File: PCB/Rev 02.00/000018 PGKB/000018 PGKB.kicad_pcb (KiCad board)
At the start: 2 copper layers, 93.5 x 72.5 mm, 140 parts, among them J1 USB Mini B, J2 BM04B-SRSS-TB, U1 SN74HCS365PWR, U2 SN74HCS365PWR, U3 SN74HCS365PWR, U4 W25Q80DVSSIG, U5 RP2040, U6 MCP1825T-3302E/DC, U7 CAT811TTBI-GT3, Y1 12 MHz

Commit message: 4L board
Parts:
- moved C27 8.23 mm to (70.3, 145.7), turned to 180 degrees
- moved C30 5.70 mm to (68.7, 137.6), turned to 0 degrees
- moved C2 0.67 mm to (89.9, 113.8)
- moved FB1 0.67 mm to (91.7, 114.0)
- moved D12 0.52 mm to (94.0, 114.0)
- moved R25 0.44 mm to (68.7, 136.1), turned to 0 degrees
- turned Y1 to 180 degrees
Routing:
- net /Main/Memory/CLK: track 0.00 -> 46.8 mm, vias 0 -> 2
- net /Main/Memory/DATA3: track 0.00 -> 46.1 mm, vias 0 -> 2
- net /Main/Memory/DATA0: track 0.00 -> 45.2 mm, vias 0 -> 2
- net /Main/Memory/DATA1: track 0.00 -> 40.9 mm, vias 0 -> 2
- net /Main/Memory/DATA2: track 0.00 -> 39.3 mm, vias 0 -> 2
- net /Main/Microcontroller/USB_MCU_D_P: track 0.00 -> 32.8 mm, vias 0 -> 2
- net /Main/Microcontroller/USB_MCU_D_N: track 0.00 -> 32.3 mm, vias 0 -> 2
- net Net-(U5-ADC_AVDD): track 4.73 -> 26.5 mm
- net /Main/USB Connector/USB_D_N: track 0.00 -> 15.4 mm
- net /Main/USB Connector/USB_D_P: track 0.00 -> 15.3 mm
- net Net-(U5-XIN): track 0.00 -> 11.5 mm
- net Net-(D10-DIN): track 0.00 -> 7.93 mm
- net GND: track 0.00 -> 7.20 mm, vias 0 -> 6
- net Net-(U5-XOUT): track 0.00 -> 3.47 mm
- added copper zone on In1.Cu, net GND
- added copper zone on In2.Cu, net GND
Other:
- copper layers 2 -> 4

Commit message: Leiskaa
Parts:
- removed FB3: Ferrite_500mA_TDK_MMZ2012Y152BT000, KD_Inductor:INDC2016X100N
- added ART1: 4-Layer Marking, KD_Mechanical:ART_4-LAYER, F.Cu at (53.4, 172.0)
- added ART2: Logo 2.5 mm Silk, KD_Mechanical:ART_LOGO_TEXT_2.5MM_SILK, F.Cu at (78.9, 172.5)
- added C3: 10n, KD_Capacitor:CAPC1608X90N, B.Cu at (81.6, 150.7)
- added R29: 10k, KD_Resistor:RESC1608X55N, B.Cu at (117.0, 115.5)
- FB2: value Ferrite_300mA_Abracon_ACML-0805-102-T -> Ferrite_500mA_TDK_MMZ2012Y152BT000
- H3: value NPTH 3.2 M3 Clearance -> NPTH_3.2; footprint KD_Mechanical_Mounting_Hole:NPTH_3.2mm_M3_clearance -> KD_Mechanical_Mounting_Hole:NPTH_3.2mm
- R15, R16, R17: value R_0603_1k_1% -> 1k
- R24: value R_0603_22k_1% -> R_0603_DNP
- R26, R27: value 4k7 -> R_0603_5100_1%; footprint KD_Resistor:RESC1005X40N -> KD_Resistor:RESC1608X55N
- TP9: moved to B.Cu
- moved C14 33.0 mm to (91.8, 142.1), turned to -90 degrees
- moved FB2 21.9 mm to (77.1, 127.0), turned to 180 degrees
- moved C41 21.7 mm to (113.3, 130.2), turned to 180 degrees
- moved R28 21.3 mm to (113.3, 128.7), turned to 0 degrees
- moved R22 20.6 mm to (53.3, 107.6), turned to 90 degrees
- moved TP2 19.4 mm to (95.8, 151.2)
- moved TP6 15.6 mm to (49.9, 126.7)
- moved R24 12.0 mm to (83.1, 150.7), turned to -90 degrees
- moved TP8 10.3 mm to (66.8, 145.2)
- moved TP14 7.02 mm to (126.4, 127.2)
- moved C32 6.70 mm to (57.7, 129.9), turned to 90 degrees
- moved TP11 4.46 mm to (66.3, 106.6)
- moved TP12 4.17 mm to (70.6, 106.6)
- moved R27 3.32 mm to (71.7, 115.8)
- moved C39 3.20 mm to (100.1, 109.1)
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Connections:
- net Net-(U5-ADC_AVDD) renamed /Main/Microcontroller/3V3_MCU
- C14 pad 1: +3.3V -> +3V3
- C15 pad 1: +3.3V -> +3V3
- J2 pad 3: /Main/Connectors/SDA -> /Main/Connectors/I2C1_SDA
- J2 pad 4: /Main/Connectors/SCL -> /Main/Connectors/I2C1_SCL
- R15 pad 1: +3.3V -> +3V3
- R16 pad 1: +3.3V -> +3V3
- R17 pad 1: +3.3V -> +3V3
- R26 pad 2: /Main/Microcontroller/SDA -> /Main/Connectors/I2C1_SDA
- R27 pad 2: /Main/Microcontroller/SCL -> /Main/Connectors/I2C1_SCL
- S1 pad 1: +3.3V -> +3V3
- S10 pad 1: +3.3V -> +3V3
- S11 pad 1: +3.3V -> +3V3
- S2 pad 1: +3.3V -> +3V3
- S3 pad 1: +3.3V -> +3V3
- S4 pad 1: +3.3V -> +3V3
- S5 pad 1: +3.3V -> +3V3
- S6 pad 1: +3.3V -> +3V3
- S7 pad 1: +3.3V -> +3V3
- S8 pad 1: +3.3V -> +3V3
- S9 pad 1: +3.3V -> +3V3
- TP11 pad 1: /Main/Microcontroller/SCL -> /Main/Connectors/I2C1_SDA
- TP12 pad 1: /Main/Microcontroller/SDA -> /Main/Connectors/I2C1_SCL
- U1 pad 16: +3.3V -> +3V3
- U2 pad 16: +3.3V -> +3V3
- U3 pad 16: +3.3V -> +3V3
- U5 pad 34: /Main/Microcontroller/I2C1_SDA -> /Main/Connectors/I2C1_SDA
- U5 pad 35: /Main/Microcontroller/I2C1_SCL -> /Main/Connectors/I2C1_SCL
- U5 pad 39: /Main/Microcontroller/GPIO10 -> /Main/Buttons/Button10
- U5 pad 40: /Main/Microcontroller/GPIO11 -> /Main/Buttons/Button11
- U6 pad 1: PERIP_~{RESET} -> /Main/Neopixel LEDs/NEOPIXEL_VDD
- U6 pad 4: Net-(U6-VO) -> +3V3
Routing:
- net +3V3: track 0.00 -> 438.0 mm, vias 0 -> 16
- net /Main/Neopixel LEDs/NEOPIXEL_VDD: track 0.00 -> 287.4 mm, vias 0 -> 12
- net GND: track 7.20 -> 138.1 mm, vias 6 -> 56
- net /Main/Memory/~{CS}_MEMORY: track 0.00 -> 112.4 mm, vias 0 -> 5
- net /Main/Microcontroller/~{RESET}: track 0.00 -> 110.2 mm, vias 0 -> 5
- net Net-(D4-DOUT): track 0.00 -> 104.3 mm, vias 0 -> 2
- net Net-(D8-DOUT): track 0.00 -> 97.6 mm, vias 0 -> 2
- net /Main/Connectors/I2C1_SDA: track 0.00 -> 63.5 mm, vias 0 -> 2
- net Net-(U1-I1): track 0.00 -> 63.3 mm, vias 0 -> 4
- net /Main/Buttons/Button8: track 0.00 -> 61.0 mm, vias 0 -> 3
- net /Main/Buttons/Button7: track 0.00 -> 59.1 mm, vias 0 -> 3
- net /Main/Connectors/I2C1_SCL: track 0.00 -> 58.7 mm, vias 0 -> 2
- net /Main/Buttons/Button4: track 0.00 -> 55.2 mm, vias 0 -> 3
- net /Main/Microcontroller/ENC_B: track 0.00 -> 54.9 mm, vias 0 -> 2
- net Net-(U3-I3): track 0.00 -> 54.4 mm, vias 0 -> 2
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- added copper zone on B.Cu, net GND
- added copper zone on F.Cu, net GND

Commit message: error fixing
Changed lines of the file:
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@@
     (property "ki_keywords" "test point testpoint")
     (attr exclude_from_pos_files exclude_from_bom)
-    (fp_text reference "TP11" (at 0 2.148) (layer "B.SilkS")
-        (effects (font (size 0.8 0.8) (thickness 0.15)) (justify mirror))
+    (fp_text reference "TP11" (at 0 -2.2) (layer "F.SilkS")
+        (effects (font (size 0.8 0.8) (thickness 0.15)))
     )
     (fp_text value "TP D2.5 mm H0.9mm" (at 0 -2.25) (layer "B.Fab") hide
@@
     (property "ki_keywords" "test point testpoint")
     (attr exclude_from_pos_files exclude_from_bom)
-    (fp_text reference "TP12" (at 0 2.148 90) (layer "B.SilkS")
-        (effects (font (size 0.8 0.8) (thickness 0.15)) (justify mirror))
+    (fp_text reference "TP12" (at 2.2 0) (layer "F.SilkS")
+        (effects (font (size 0.8 0.8) (thickness 0.15)))
     )
     (fp_text value "TP D2.5 mm H0.9mm" (at 0 -2.25 90) (layer "B.Fab") hide
@@
     (property "ki_keywords" "test point testpoint")
     (attr exclude_from_pos_files exclude_from_bom)
-    (fp_text reference "TP7" (at 0 2.148 90) (layer "B.SilkS")
+    (fp_text reference "TP7" (at 2.300674 -0.950211 -180) (layer "B.SilkS")
         (effects (font (size 0.8 0.8) (thickness 0.15)) (justify mirror))
     )
@@
         (effects (font (size 0.5 0.5) (thickness 0.1)) (justify mirror))
     )
-    (fp_line (start -1.62 -8.73) (end 7.57 -8.73)
-      (stroke (width 0.12) (type solid)) (layer "B.SilkS"))
-    (fp_line (start -1.62 -6) (end -1.62 -8.73)
-      (stroke (width 0.12) (type solid)) (layer "B.SilkS"))
     (fp_line (start -1.62 -2.4) (end -1.62 -3.3)
       (stroke (width 0.12) (type solid)) (layer "B.SilkS"))
     (fp_line (start -1.5 0.68) (end 7.45 0.68)
       (stroke (width 0.12) (type solid)) (layer "B.SilkS"))
-    (fp_line (start 7.57 -6) (end 7.57 -8.73)
-      (stroke (width 0.12) (type solid)) (layer "B.SilkS"))
     (fp_line (start 7.57 -2.4) (end 7.57 -3.3)
       (stroke (width 0.12) (type solid)) (layer "B.SilkS"))
@@
     (fp_line (start -1.5 -8.61) (end 7.45 -8.61)
       (stroke (width 0.1) (type solid)) (layer "B.Fab"))
+    (fp_line (start -1.5 -6.1) (end 1 -6.1)
+      (stroke (width 0.1) (type dot)) (layer "B.Fab"))
     (fp_line (start -1.5 0.56) (end -1.5 -8.61)
       (stroke (width 0.1) (type solid)) (layer "B.Fab"))
     (fp_line (start -1.5 0.56) (end 7.45 0.56)
       (stroke (width 0.1) (type solid)) (layer "B.Fab"))
-    (fp_line (start -0.025 -6.1) (end 5.975 -6.1)
-      (stroke (width 0.1) (type solid)) (layer "B.Fab"))
+    (fp_line (start 5 -6.1) (end 7.5 -6.1)
+      (stroke (width 0.1) (type dot)) (layer "B.Fab"))
     (fp_line (start 7.45 0.56) (end 7.45 -8.61)
       (stroke (width 0.1) (type solid)) (layer "B.Fab"))
@@
     (property "ki_keywords" "test point testpoint")
     (attr exclude_from_pos_files exclude_from_bom)
-    (fp_text reference "TP14" (at 0 2.148 270) (layer "B.SilkS")
+    (fp_text reference "TP14" (at -1 -3) (layer "B.SilkS")
         (effects (font (size 0.8 0.8) (thickness 0.15)) (justify mirror))
     )
@@
     (property "ki_keywords" "test point testpoint")
     (attr exclude_from_pos_files exclude_from_bom)
-    (fp_text reference "TP2" (at 0 2.148 90) (layer "B.SilkS")
+    (fp_text reference "TP2" (at -2.2 0.7 -180) (layer "B.SilkS")
         (effects (font (size 0.8 0.8) (thickness 0.15)) (justify mirror))
     )
@@
     (property "ki_keywords" "test point testpoint")
     (attr exclude_from_pos_files exclude_from_bom)
-    (fp_text reference "TP16" (at 0 2.148) (layer "B.SilkS")
+    (fp_text reference "TP16" (at -0.1 -2.3) (layer "B.SilkS")
         (effects (font (size 0.8 0.8) (thickness 0.15)) (justify mirror))
     )
@@
     (property "ki_keywords" "test point testpoint")
     (attr exclude_from_pos_files exclude_from_bom)
-    (fp_text reference "TP3" (at 0 2.148) (layer "B.SilkS")
+    (fp_text reference "TP3" (at 2.3 1.8) (layer "B.SilkS")
         (effects (font (size 0.8 0.8) (thickness 0.15)) (justify mirror))
     )
@@
         (xy 59.5 123)
         (xy 59.5 127)
-        (xy 59.5 127)
       )

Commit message: layout
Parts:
- C16, C17, C18: value C_0603_100n_X7R_50V -> 100n
- FD1, FD2, FD3, FD4, FD5, FD6: value Fiducial_0.5mm -> Fiducial 0.5 mm
- S12, S13: value Button_tactile_45x38_430181038816 -> 430181038816
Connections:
- U3 pad 10: unconnected-(U3-I4-Pad10) -> GND
- U3 pad 12: unconnected-(U3-I5-Pad12) -> GND
- U3 pad 14: unconnected-(U3-I6-Pad14) -> GND
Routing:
- net GND: track 138.1 -> 145.4 mm, vias 56 -> 57

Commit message: päivityksiä
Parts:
- added R30: 100k, KD_Resistor:RESC1608X55N, B.Cu at (161.6, 132.4)
- added R31: 100k, KD_Resistor:RESC1608X55N, B.Cu at (161.6, 134.9)
- added R34: 100k, KD_Resistor:RESC1608X55N, B.Cu at (161.6, 137.4)
- added R35: 100k, KD_Resistor:RESC1608X55N, B.Cu at (161.6, 139.9)
- added R36: 100k, KD_Resistor:RESC1608X55N, B.Cu at (161.6, 142.4)
- added R37: 100k, KD_Resistor:RESC1608X55N, B.Cu at (161.6, 144.9)
- added R38: 100k, KD_Resistor:RESC1608X55N, B.Cu at (157.6, 132.4)
- added R39: 100k, KD_Resistor:RESC1608X55N, B.Cu at (157.6, 134.9)
- added R40: 100k, KD_Resistor:RESC1608X55N, B.Cu at (157.6, 137.4)
- added R41: 100k, KD_Resistor:RESC1608X55N, B.Cu at (157.6, 139.9)
- added R42: 100k, KD_Resistor:RESC1608X55N, B.Cu at (157.6, 142.4)
- moved R2 3.11 mm to (80.8, 108.4)
- moved R1 3.11 mm to (82.4, 108.4)
- moved C21 0.90 mm to (76.6, 107.5)
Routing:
- net /Main/USB Connector/CC1: track 11.8 -> 8.97 mm
- net /Main/USB Connector/CC2: track 9.28 -> 11.0 mm
- net +3V3: track 438.0 -> 437.1 mm
- net GND: track 145.4 -> 145.3 mm, vias 57 -> 181

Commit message: Review checklists
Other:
- board text added: "000018 PGKB Rev 1.00"
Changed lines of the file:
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@@
     (fp_arc (start 0.833601 0.096099) (mid 0.973613 -0.257639) (end 1.31605 -0.423381)
       (stroke (width 0.2) (type solid)) (layer "F.SilkS"))
-    (fp_arc (start 1.31605 -0.683114) (mid 1.907699 -0.405492) (end 2.078018 0.225468)
+    (fp_arc (start 1.31605 -0.683114) (mid 1.907695 -0.405492) (end 2.078018 0.225468)
       (stroke (width 0.2) (type solid)) (layer "F.SilkS"))
     (fp_arc (start 1.31605 -0.423379) (mid 1.645394 -0.271037) (end 1.761468 0.072768)
@@
     (fp_arc (start 1.355618 1.232463) (mid 0.731987 0.965619) (end 0.50639 0.325909)
       (stroke (width 0.2) (type solid)) (layer "F.SilkS"))
-    (fp_arc (start 1.372869 0.972724) (mid 0.966364 0.781549) (end 0.82295 0.35584)
+    (fp_arc (start 1.372869 0.972724) (mid 0.966366 0.781547) (end 0.82295 0.35584)
       (stroke (width 0.2) (type solid)) (layer "F.SilkS"))
     (fp_arc (start 1.8609 0.725158) (mid 1.647116 0.90854) (end 1.372868 0.972731)
@@
     (fp_arc (start 3.12764 0.972723) (mid 2.834729 0.892832) (end 2.685781 0.628268)
       (stroke (width 0.2) (type solid)) (layer "F.SilkS"))
-    (fp_arc (start 3.12764 1.232463) (mid 2.619347 1.092399) (end 2.369218 0.628268)
+    (fp_arc (start 3.12764 1.232463) (mid 2.61934 1.092397) (end 2.369218 0.628268)
       (stroke (width 0.2) (type solid)) (layer "F.SilkS"))
-    (fp_arc (start 5.03409 0.259459) (mid 5.19195 -0.37288) (end 5.765118 -0.683118)
+    (fp_arc (start 5.03409 0.259459) (mid 5.191951 -0.372877) (end 5.765118 -0.683118)
       (stroke (width 0.2) (type solid)) (layer "F.SilkS"))
     (fp_arc (start 5.761569 1.232466) (mid 5.184943 0.905126) (end 5.03409 0.259459)
@@
     (fp_arc (start 5.844259 -0.423382) (mid 6.101988 -0.353589) (end 6.28105 -0.155518)
       (stroke (width 0.2) (type solid)) (layer "F.SilkS"))
-    (fp_arc (start 6.280538 1.013814) (mid 6.045436 1.181008) (end 5.761568 1.232468)
+    (fp_arc (start 6.280538 1.013814) (mid 6.045436 1.181019) (end 5.761568 1.232468)
       (stroke (width 0.2) (type solid)) (layer "F.SilkS"))
     (fp_arc (start 6.280541 1.169557) (mid 6.145913 1.523237) (end 5.79099 1.65455)
@@
     (fp_arc (start 7.400665 -0.416784) (mid 7.646446 -0.616044) (end 7.955659 -0.683118)
       (stroke (width 0.2) (type solid)) (layer "F.SilkS"))
-    (fp_arc (start 7.407765 -0.124568) (mid 7.589656 -0.340694) (end 7.859781 -0.423381)
+    (fp_arc (start 7.407765 -0.124568) (mid 7.589655 -0.340729) (end 7.859781 -0.423381)
       (stroke (width 0.2) (type solid)) (layer "F.SilkS"))
     (fp_arc (start 7.859779 -0.42338) (mid 8.138248 -0.314437) (end 8.231131 -0.030218)
       (stroke (width 0.2) (type solid)) (layer "F.SilkS"))
-    (fp_arc (start 7.955657 -0.683113) (mid 8.404847 -0.489303) (end 8.54819 -0.02159)
+    (fp_arc (start 7.955657 -0.683113) (mid 8.404805 -0.489301) (end 8.54819 -0.02159)
       (stroke (width 0.2) (type solid)) (layer "F.SilkS"))
     (fp_arc (start 9.023535 -0.141819) (mid 9.255576 -0.552139) (end 9.7084 -0.683118)
@@
     (fp_arc (start 9.708398 -0.683125) (mid 10.188203 -0.5481) (end 10.415081 -0.104281)
       (stroke (width 0.2) (type solid)) (layer "F.SilkS"))
-    (fp_arc (start 9.708398 -0.423378) (mid 9.96879 -0.344297) (end 10.097 -0.104281)
+    (fp_arc (start 9.708398 -0.423378) (mid 9.968762 -0.344292) (end 10.097 -0.104281)
       (stroke (width 0.2) (type solid)) (layer "F.SilkS"))
     (fp_arc (start 9.71855 0.972726) (mid 9.425639 0.892824) (end 9.276681 0.628268)
       (stroke (width 0.2) (type solid)) (layer "F.SilkS"))
-    (fp_arc (start 9.71855 1.232464) (mid 9.21027 1.092398) (end 8.960131 0.628268)
+    (fp_arc (start 9.71855 1.232464) (mid 9.210242 1.092402) (end 8.960131 0.628268)
       (stroke (width 0.2) (type solid)) (layer "F.SilkS"))
   )
@@
     (effects (font (size 1 1) (thickness 0.15)) (justify left bottom))
   )
+  (gr_text "000018 PGKB Rev 1.00" (at 98.5 172.2) (layer "F.SilkS")
+    (effects (font (size 1 1) (thickness 0.15)) (justify left bottom))
+  )

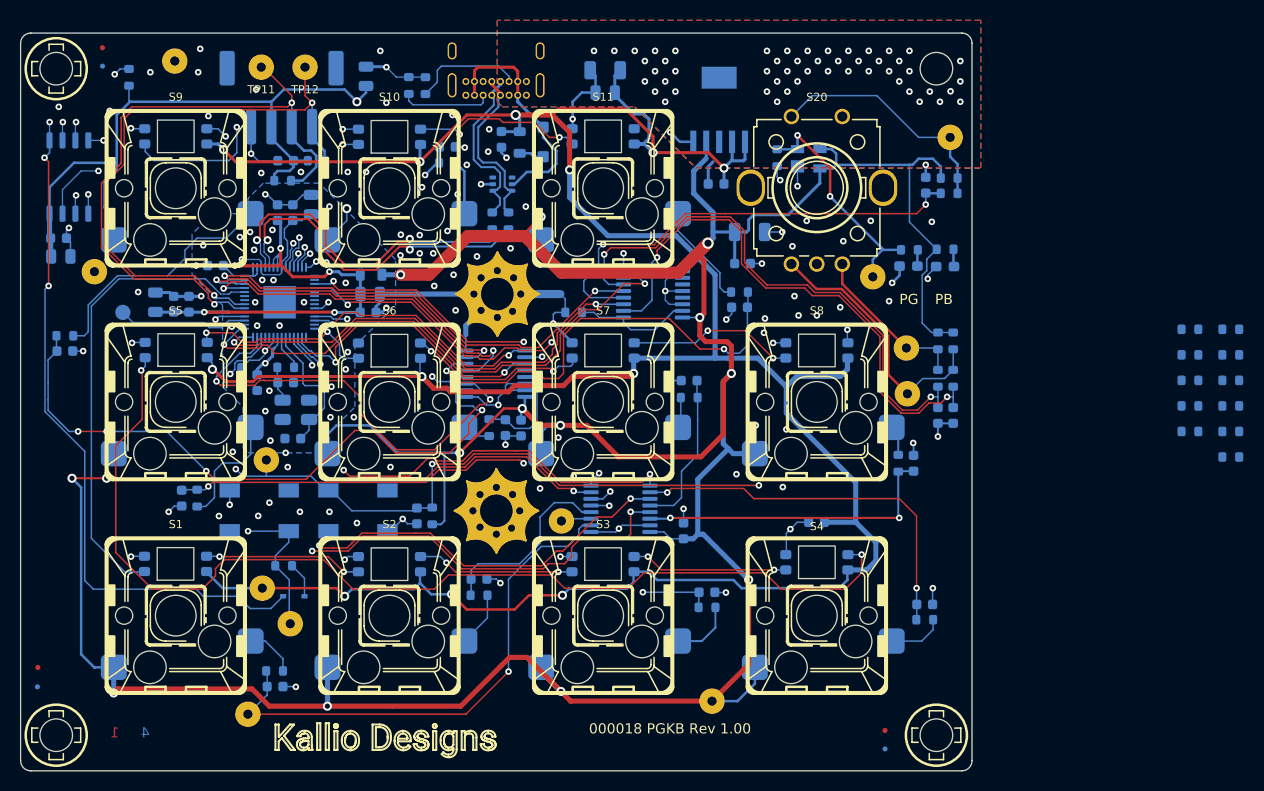
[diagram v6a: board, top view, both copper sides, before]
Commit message: USB connector moved
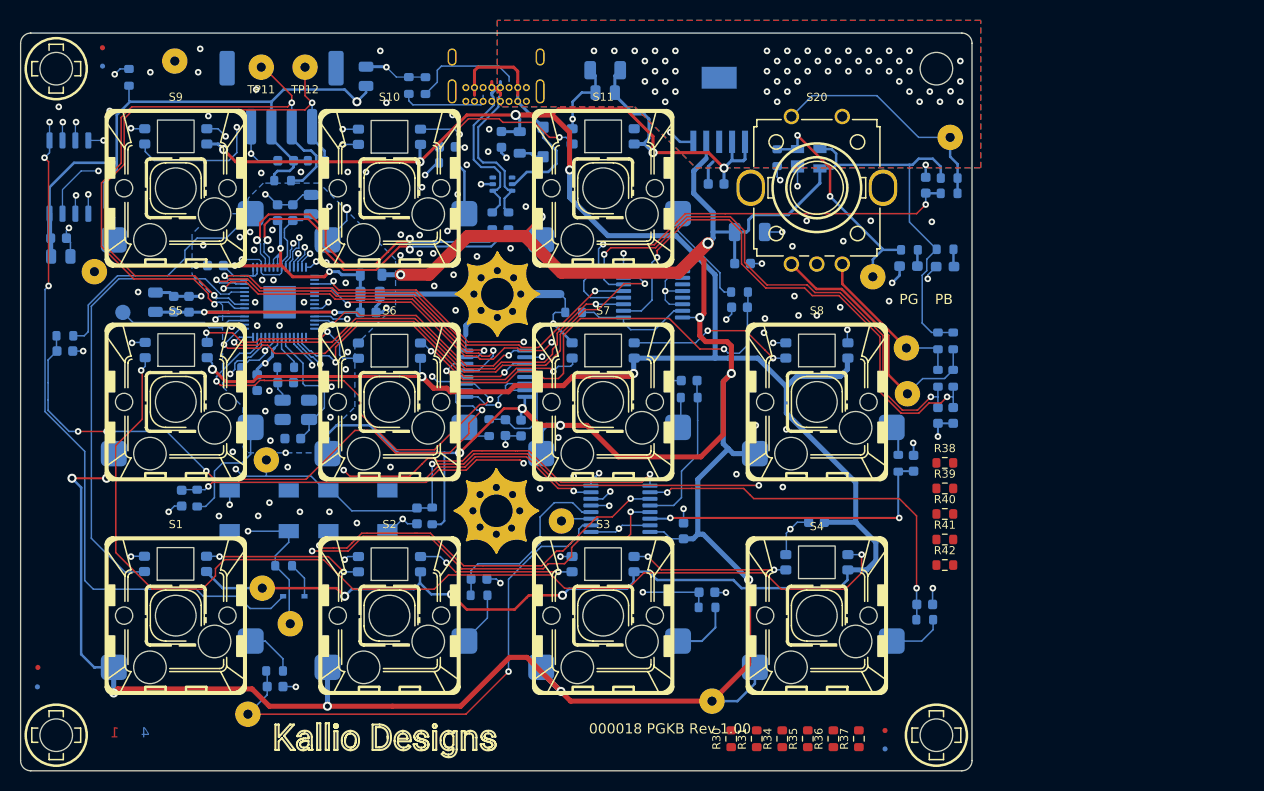
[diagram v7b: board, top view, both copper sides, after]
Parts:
- R30, R31, R34, R35, R36, R37, R38, R39, R40, R41, R42: moved to F.Cu
- moved R30 63.5 mm to (112.5, 172.6), turned to 90 degrees
- moved R31 59.9 mm to (115.0, 172.6), turned to 90 degrees
- moved R34 56.4 mm to (117.5, 172.6), turned to 90 degrees
- moved R35 52.9 mm to (120.0, 172.6), turned to 90 degrees
- moved R36 49.4 mm to (122.5, 172.6), turned to 90 degrees
- moved R37 45.9 mm to (125.0, 172.6), turned to 90 degrees
- moved R41 27.4 mm to (133.5, 153.0), turned to 0 degrees
- moved R38 27.4 mm to (133.5, 145.5), turned to 0 degrees
- moved R39 27.4 mm to (133.5, 148.0), turned to 0 degrees
- moved R40 27.4 mm to (133.5, 150.5), turned to 0 degrees
- moved R42 27.4 mm to (133.5, 155.5), turned to 0 degrees
- moved J1 0.60 mm to (86.4, 110.0)
